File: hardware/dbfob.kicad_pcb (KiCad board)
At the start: 2 copper layers, 30 x 52.5 mm, 17 parts, among them J1 PROG, SW1 measure, U1 CH32V003F4P6

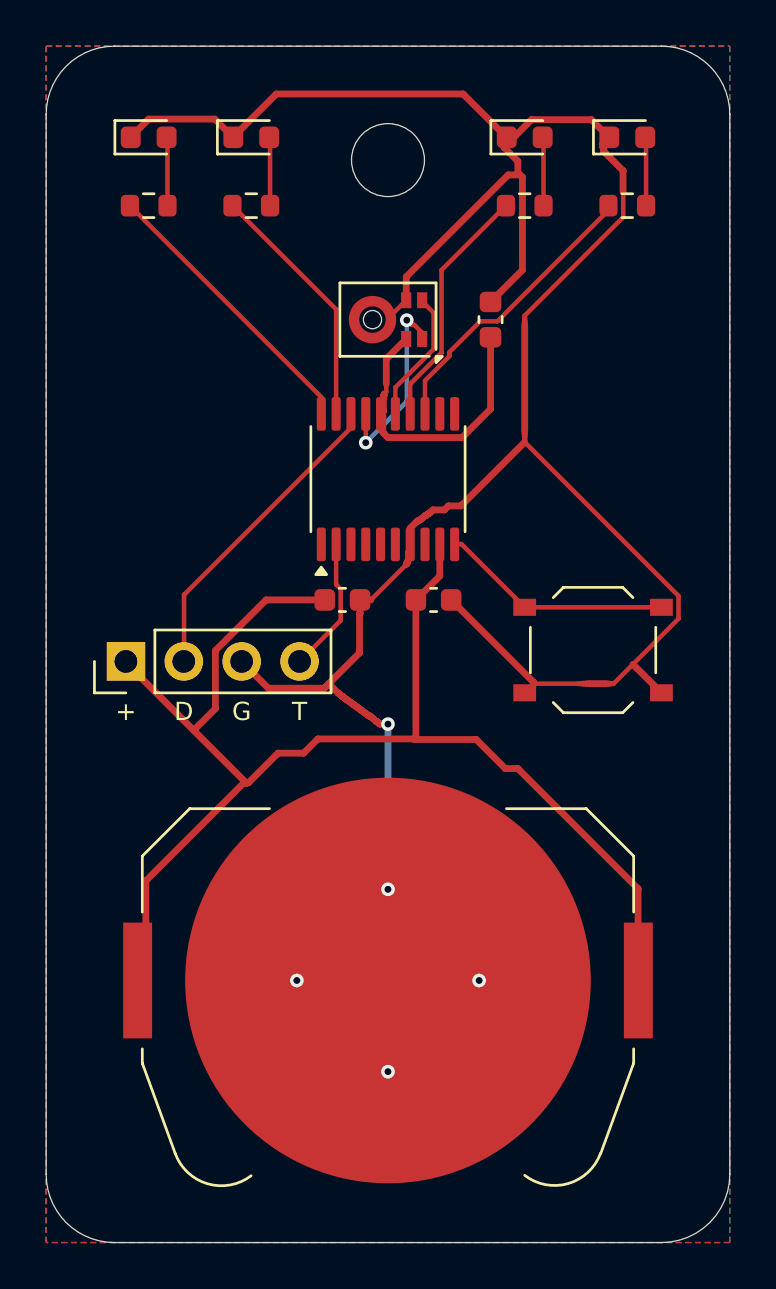
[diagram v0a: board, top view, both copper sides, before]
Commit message: hardware: dim LED bar, D4 doubles as ambient light sensor
Resistors 2.2k (1k for the dimmer yellow-green) cap the LEDs at
~0.45-1 mA; a club is dark and the bar should not light the room.
D4's cathode moves from GND to PC2 so the red LED can be reverse-biased
and timed as a light sensor: auto-dim indoors, brighter in daylight,
no extra part. Rerouted: DRC/parity clean, CPL check passes.

Co-Authored-By: Claude Opus 5.5 <noreply@anthropic.com>
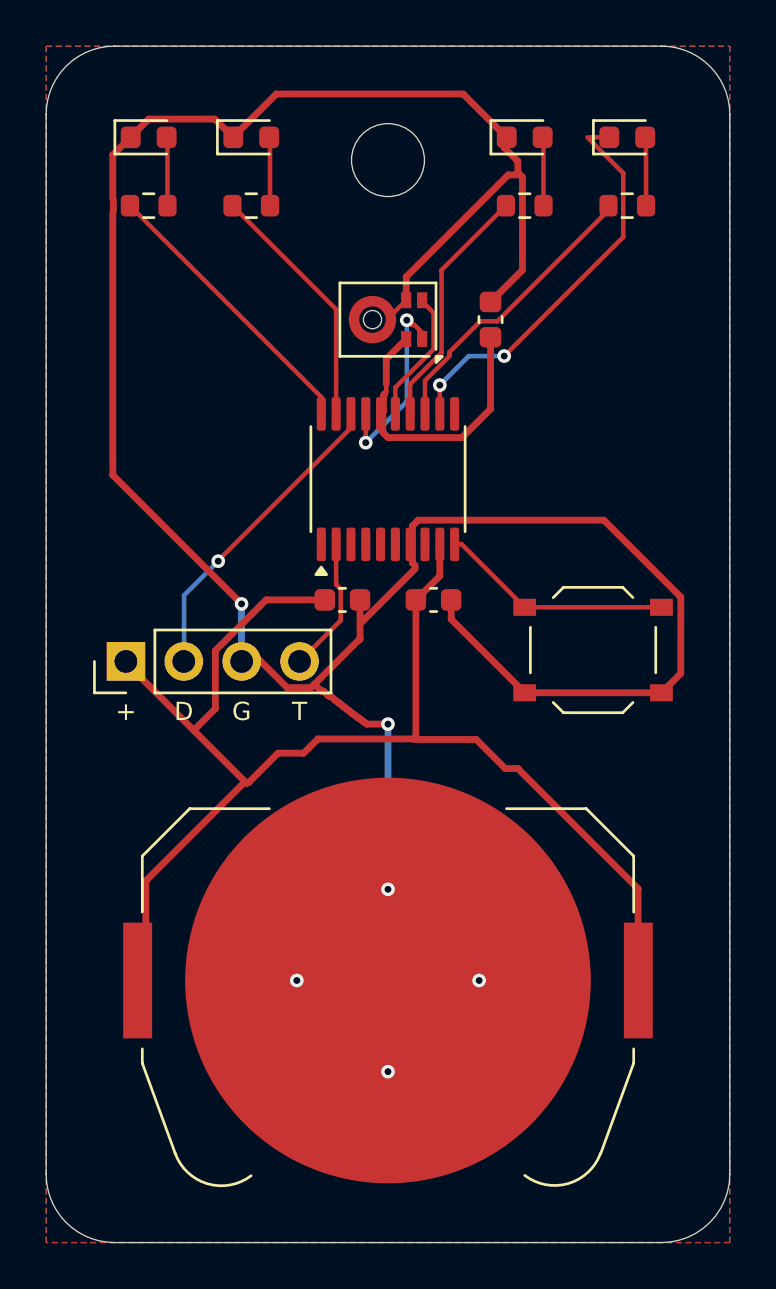
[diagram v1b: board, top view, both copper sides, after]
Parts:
- R4: value 220 -> 1k
- R5, R6, R7: value 470 -> 2.2k
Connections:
- D4 pad 1: /GND -> /LED_R_K
- U1 pad 12: unconnected-(U1-PC2-Pad12) -> /LED_R_K
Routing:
- net /LED_R_K: track 0.00 -> 17.7 mm, vias 0 -> 2
- net /GND: track 113.6 -> 117.3 mm, vias 5 -> 6
- net /SWIO: vias 0 -> 1

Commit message: Show bare-ear and with-plugs verdicts together
Either default misleads someone: assume plugs and the unprotected get a
falsely safe answer; assume none and plug wearers always see red. Every
reading now shows both - steady LED for a bare ear, blinking LED for
room level minus 12 dB - so there is no mode to set or forget. Bands are
redefined as level at the ear (G<=83 Y<=90 O<=96 R>96 dBA); back-silk
legend updated to match. No circuit change.

Co-Authored-By: Claude Opus 5.5 <noreply@anthropic.com>
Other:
- board text added: "G<=83 Y<=90 O<=96 R>96"
- board text added: "blink = with plugs"
- board text added: "dBA at ear CERN-OHL-P"
- board text added: "steady = bare ear"
- board text removed: "CERN-OHL-P"
- board text removed: "G <=95 Y <=102"
- board text removed: "O <=108 R >108 dBA"
- board text removed: "with ~12 dB earplugs"
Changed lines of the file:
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@@
 		)
 	)
-	(gr_text "with ~12 dB earplugs"
+	(gr_text "G<=83 Y<=90 O<=96 R>96"
 		(at 115 148.2 0)
 		(layer "B.SilkS")
@@
 		)
 	)
-	(gr_text "CERN-OHL-P"
+	(gr_text "dBA at ear  CERN-OHL-P"
 		(at 115 150 0)
 		(layer "B.SilkS")
@@
 		)
 	)
-	(gr_text "G <=95  Y <=102"
+	(gr_text "steady = bare ear"
 		(at 115 133.6 0)
 		(layer "B.SilkS")
@@
 		)
 	)
-	(gr_text "O <=108  R >108 dBA"
+	(gr_text "blink = with plugs"
 		(at 115 135.2 0)
 		(layer "B.SilkS")

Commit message: Address hardware audit: clock plan, claims, power, release gates
- PDM clock 1.024 MHz sat between the IM69D130's specified bands and
  cannot be divided from 48 MHz; now 1.5 MHz (48/32 or 24/16),
  decimated by 64 to 23,437.5 samples/s.
- Bands restated as levels at the ear with allowance times from the
  stated curve (96 dBA = 38 min, not an hour); the plugs LED is a
  conditional estimate, not a safety verdict. Silk legend updated.
- Power: unsupported 10-15% capacity claim withdrawn; qualification
  plan, under-load cutoff, standby budget (V003 7.6 uA ~ 67 mAh/yr).
- Programming: remove the cell first (J1 pin 1 is the cell's +);
  back silk, schematic note and README say so.
- make_pcb.py and fab.py now fail on any ERC/DRC/parity finding beyond
  the documented ones; fab.py stages outputs and publishes only after
  check_cpl.py passes, which now also checks BOM/CPL membership,
  duplicates and layer.
- Mic lifecycle recorded as unresolved (DigiKey: Active).

Co-Authored-By: Claude Opus 5.5 <noreply@anthropic.com>
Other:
- board text added: "G<=83 Y<=90 O<=96 R>=97"
- board text added: "REMOVE CELL TO PROGRAM"
- board text added: "blink = plugs IF 12 dB"
- board text removed: "G<=83 Y<=90 O<=96 R>96"
- board text removed: "blink = with plugs"
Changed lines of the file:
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@@
 		)
 	)
-	(gr_text "G<=83 Y<=90 O<=96 R>96"
+	(gr_text "G<=83 Y<=90 O<=96 R>=97"
 		(at 115 148.2 0)
 		(layer "B.SilkS")
@@
 		)
 	)
+	(gr_text "REMOVE CELL TO PROGRAM"
+		(at 118 123.4 0)
+		(layer "B.SilkS")
+		(effects
+			(font
+				(size 0.8 0.8)
+				(thickness 0.15)
+			)
+			(justify mirror)
+		)
+	)
 	(gr_text "steady = bare ear"
 		(at 115 133.6 0)
@@
 		)
 	)
-	(gr_text "blink = with plugs"
+	(gr_text "blink = plugs IF 12 dB"
 		(at 115 135.2 0)
 		(layer "B.SilkS")
